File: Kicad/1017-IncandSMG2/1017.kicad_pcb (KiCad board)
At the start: 2 copper layers, 44.4 x 20.3 mm, 40 parts, among them P1 CONN_4, P2 CONN_8, P3 CONN_4, P4 SPADE_187, P5 CONN_2, P6 TST, P7 CONN_8, Q1 MOSFET_N, Q10 MOSFET_N, Q11 MOSFET_N, Q12 MOSFET_N, Q13 MOSFET_N, Q14 MOSFET_N, Q15 MOSFET_N, Q16 MOSFET_N, Q17 MOSFET_N, Q18 MOSFET_N, Q19 MOSFET_N, Q2 MOSFET_N, Q20 MOSFET_N, Q21 MOSFET_N, Q22 MOSFET_N, Q23 MOSFET_N, Q24 MOSFET_N, Q3 MOSFET_N, Q4 MOSFET_N, Q5 MOSFET_N, Q6 MOSFET_N, Q7 MOSFET_N, Q8 MOSFET_N, Q9 MOSFET_N

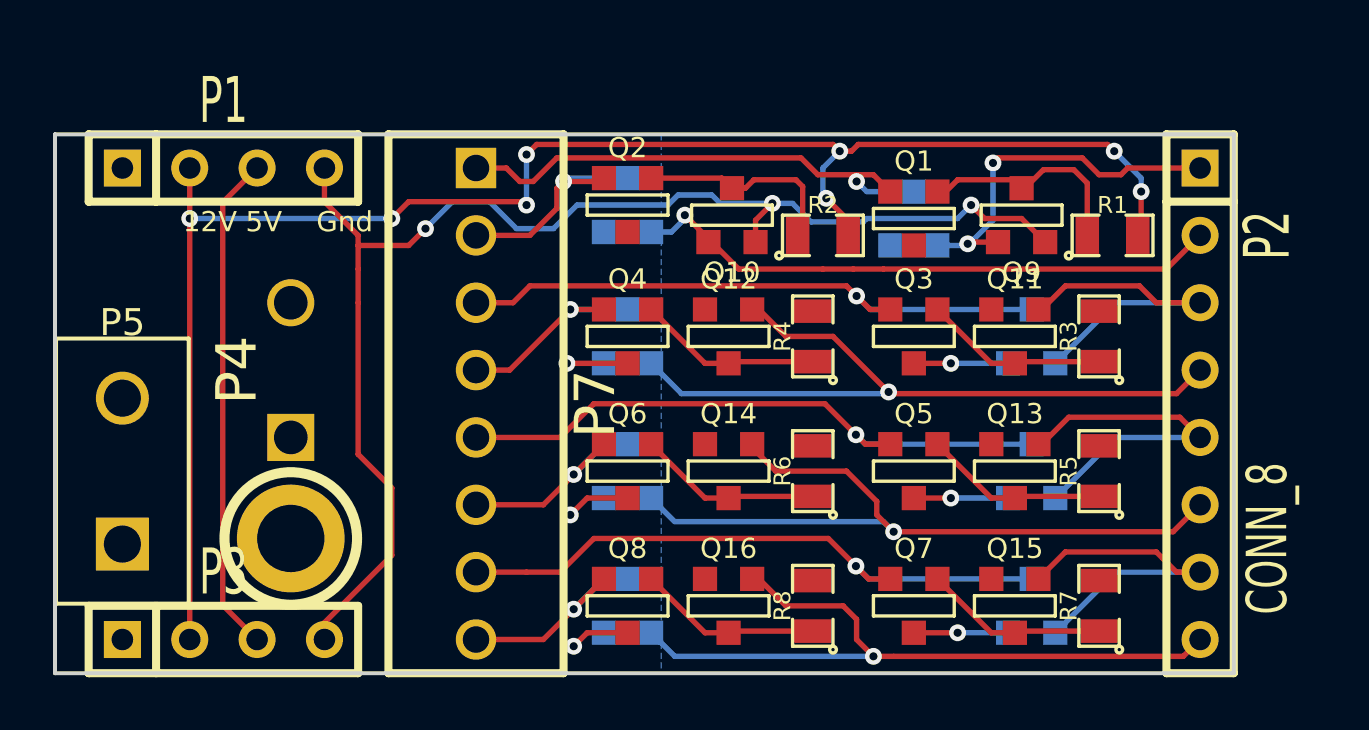
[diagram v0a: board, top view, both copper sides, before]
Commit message: Gen2 Firmware: Added Gen2.rev0.1.0.0.cyacd as first official OPP Gen2 firmware image.
Kicad:
Finished surface mount Gen2 layout.  Created panelized PCB for ITeadStudio order.
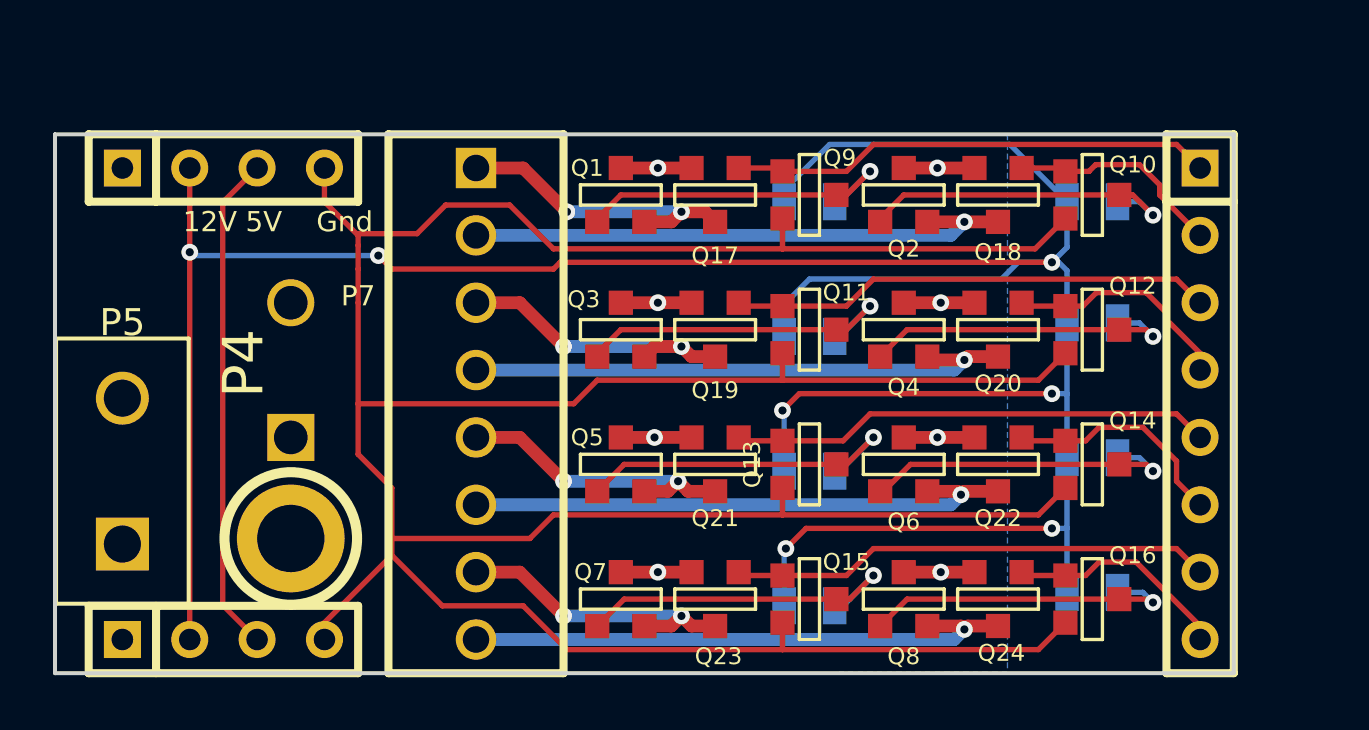
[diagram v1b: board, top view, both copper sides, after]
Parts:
- Q17, Q18, Q19, Q20, Q21, Q22, Q23, Q24: moved to F.Cu
- R1, R2, R3, R4, R5, R6, R7, R8: moved to B.Cu
- moved Q18 14.0 mm to (134.6, 69.6)
- moved Q20 14.0 mm to (134.6, 74.7)
- moved Q22 14.0 mm to (134.6, 79.8)
- moved Q24 14.0 mm to (134.6, 84.8)
- moved Q12 13.7 mm to (138.2, 74.7), turned to 90 degrees
- moved Q14 13.7 mm to (138.2, 79.8), turned to 90 degrees
- moved Q16 13.7 mm to (138.2, 84.8), turned to 90 degrees
- moved Q10 13.6 mm to (138.2, 69.6), turned to 90 degrees
- moved Q19 11.9 mm to (124.0, 74.7)
- moved Q21 11.9 mm to (124.0, 79.8)
- moved Q23 11.9 mm to (124.0, 84.8)
- moved R1 11.5 mm to (127.5, 69.8), turned to 180 degrees
- moved Q1 11.1 mm to (120.4, 69.6), turned to 180 degrees
- moved Q3 11.1 mm to (120.4, 74.7), turned to 180 degrees
- moved Q5 11.1 mm to (120.4, 79.8), turned to 180 degrees
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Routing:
- net GND: track 50.4 -> 133.4 mm, vias 3 -> 0
- net +12V1: track 62.8 -> 117.3 mm, vias 8 -> 7
- net /P5: track 28.7 -> 8.65 mm, vias 1 -> 0
- net /P3: track 28.2 -> 8.72 mm, vias 1 -> 0
- net /P7: track 27.6 -> 8.50 mm, vias 1 -> 0
- net /P1: track 22.5 -> 8.22 mm, vias 1 -> 0
- net N-0000011: track 7.93 -> 21.3 mm
- net N-000007: track 8.28 -> 21.3 mm
- net N-000009: track 8.28 -> 21.2 mm
- net N-0000016: track 8.63 -> 21.3 mm
- net N-0000010: track 23.6 -> 11.3 mm, vias 1 -> 2
- net N-000008: track 23.6 -> 11.4 mm, vias 1 -> 2
- net N-0000024: track 23.1 -> 11.4 mm, vias 1 -> 2
- net N-0000022: track 19.3 -> 11.4 mm, vias 1 -> 2
- net N-0000014: track 6.96 -> 13.2 mm, vias 0 -> 1
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
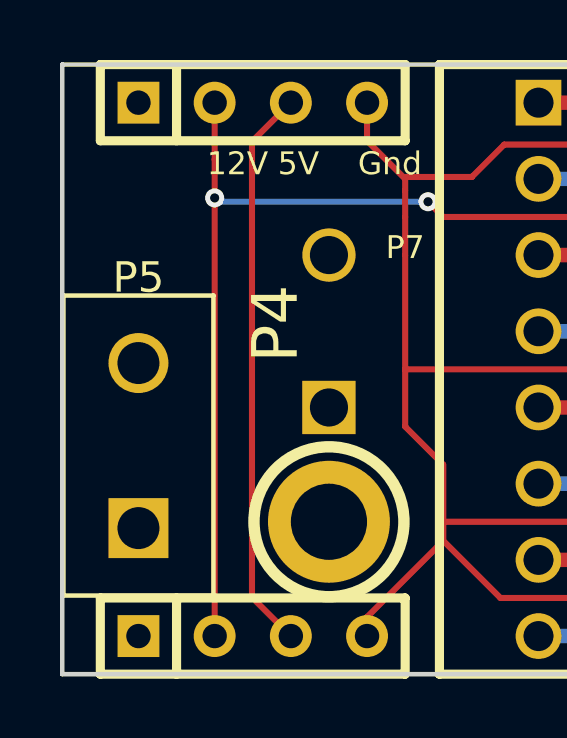
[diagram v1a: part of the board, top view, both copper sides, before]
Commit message: Gen2 embedded code: Remove debug code that always overwrites NV configuration.  Added Gen2.rev0.1.1.0.cyacd for downloading to boards.
PopulateBrd document:
Correct solenoid pinout picture.

SolDrvG2 board:
Move location of 4 pin switch input header to reduce interference with interface board.  Update to use cheaper 6 pin Molex header.  Add rev to copper layer.

IntfBrdG2 board:
Change future pin on ribbon cable connector to carry 12V.  Make board slightly larger so it can be panellized by IteadStudio.  Add better grounding.  Move ribbon cable connectors so less interference with solenoid board input header.  Add 3 pin header to make communicating with first board in chain easier (switch comms between 4 pin header and ribbon cable).  Add rev to copper layer.

IncandSMG2 board:
Update to use cheaper 2 pin Molex header.  Add rev to copper layer.

Panellize Gerbers:
Add panellized boards for SolDrvG2, IntfBrdG2, and IncandSMG2.

MPF/SS3:
Small updates to add skillshot.
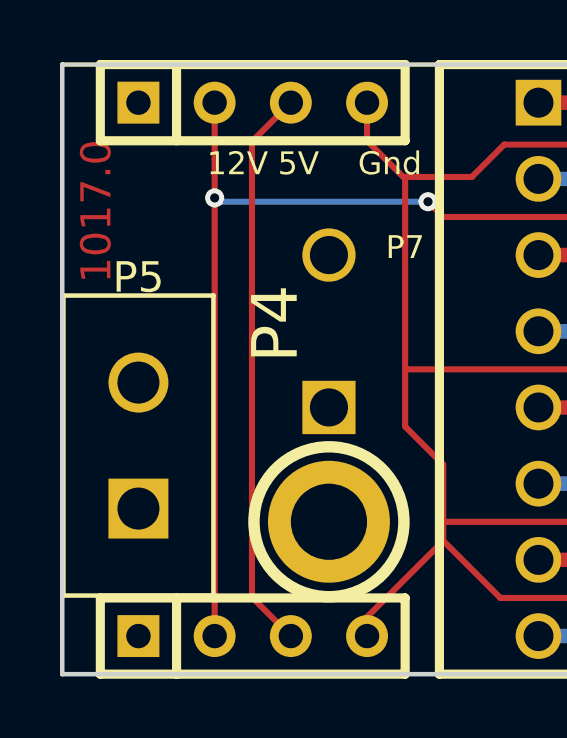
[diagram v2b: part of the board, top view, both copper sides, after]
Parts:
- P5: footprint 00_th1x2x4.2mm_nopeg -> 00_th1x2x4.2mm_cheap
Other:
- board text added: "1017.0"
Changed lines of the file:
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@@
     (area 98.035534 65.910884 143.865601 88.521116)
     (thickness 1.6)
-    (drawings 7)
+    (drawings 8)
     (tracks 292)
     (zones 0)
@@
     )
   )
-  (module 00_th1x2x4.2mm_nopeg (layer F.Cu)
-    (at 101.6 80.01)
-    (descr "Double rangee de contacts 2 x 8 pins")
-    (tags CONN)
-    (fp_text reference P5 (at 0 -5.6007) (layer F.SilkS)
-      (effects (font (size 1.016 1.016) (thickness 0.2032)))
-    )
-    (fp_text value CONN_2 (at 0.127 0.127) (layer F.SilkS) hide
-      (effects (font (size 1.016 1.016) (thickness 0.2032)))
-    )
-    (fp_line (start -2.5 -5) (end 2.5 -5) (layer F.SilkS) (width 0.15))
-    (fp_line (start 2.5 -5) (end 2.5 5) (layer F.SilkS) (width 0.15))
-    (fp_line (start 2.5 5) (end -2.5 5) (layer F.SilkS) (width 0.15))
-    (fp_line (start -2.5 5) (end -2.5 -5) (layer F.SilkS) (width 0.15))
-    (pad 1 thru_hole rect (at 0 2.75082) (size 1.99898 1.99898) (drill 1.39954)
-      (layers *.Cu *.Mask F.SilkS)
-      (net 3 +VLED)
-    )
-    (pad 2 thru_hole circle (at 0 -2.75082) (size 1.99898 1.99898) (drill 1.39954)
-      (layers *.Cu *.Mask F.SilkS)
-      (net 3 +VLED)
-    )
-    (model pin_array/pins_array_8x2.wrl
-      (at (xyz 0 0 0))
-      (scale (xyz 1 1 1))
-      (rotate (xyz 0 0 0))
-    )
-  )
   (module 00_th1x2x200 (layer F.Cu)
     (at 107.95 76.2 90)
@@
     )
   )
+  (module 00_th1x2x4.2mm_cheap (layer F.Cu)
+    (at 101.6 80.01)
+    (descr "Double rangee de contacts 2 x 8 pins")
+    (tags CONN)
+    (fp_text reference P5 (at 0 -5.6007) (layer F.SilkS)
+      (effects (font (size 1.016 1.016) (thickness 0.2032)))
+    )
+    (fp_text value CONN_2 (at 0.127 0.127) (layer F.SilkS) hide
+      (effects (font (size 1.016 1.016) (thickness 0.2032)))
+    )
+    (fp_line (start -2.5 -5) (end 2.5 -5) (layer F.SilkS) (width 0.15))
+    (fp_line (start 2.5 -5) (end 2.5 5) (layer F.SilkS) (width 0.15))
+    (fp_line (start 2.5 5) (end -2.5 5) (layer F.SilkS) (width 0.15))
+    (fp_line (start -2.5 5) (end -2.5 -5) (layer F.SilkS) (width 0.15))
+    (pad 1 thru_hole rect (at 0 2.1) (size 1.99898 1.99898) (drill 1.39954)
+      (layers *.Cu *.Mask F.SilkS)
+      (net 3 +VLED)
+    )
+    (pad 2 thru_hole circle (at 0 -2.1) (size 1.99898 1.99898) (drill 1.39954)
+      (layers *.Cu *.Mask F.SilkS)
+      (net 3 +VLED)
+    )
+    (model pin_array/pins_array_8x2.wrl
+      (at (xyz 0 0 0))
+      (scale (xyz 1 1 1))
+      (rotate (xyz 0 0 0))
+    )
+  )
+  (gr_text 1017.0 (at 100.2 72.2 90) (layer F.Cu)
+    (effects (font (size 1 1) (thickness 0.25)))
+  )
   (gr_text Gnd (at 109.982 70.612) (layer F.SilkS)
